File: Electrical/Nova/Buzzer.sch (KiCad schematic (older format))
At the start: 2 parts, among them IC1201 74HC2GU04GW,125

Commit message: Deleted Inverter
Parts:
- removed IC1201: 74HC2GU04GW,125, Footprint Library:SOP65P210X110-6N, symbol Nova-rescue:74HC2GU04GW,125-74HC2GU04GW_125-Nova-rescue-Nova-rescue-Nova-rescue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
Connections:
- net labels removed: +3V3
- wire segments 15 -> 2
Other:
- moved on the sheet: LS1201
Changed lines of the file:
@@
 $Descr A4 11693 8268
 encoding utf-8
-Sheet 12 19
+Sheet 3 19
 Title ""
 Date ""
@@
 L Nova-rescue:PS1440P02BT-PS1440P02BT-Nova-rescue-Nova-rescue-Nova-rescue-Nova-rescue-Nova-rescue LS1201
 U 1 1 5F404605
-P 5450 3800
-F 0 "LS1201" H 5580 3846 50  0000 L CNN
-F 1 "PS1440P02BT" H 5580 3755 50  0000 L CNN
-F 2 "Footprint Library:BUZZER_PS1440P02BT" H 5450 3800 50  0001 L BNN
-F 3 "https://product.tdk.com/info/en/catalog/datasheets/piezoelectronic_buzzer_ps_en.pdf" H 5450 3800 50  0001 L BNN
-F 4 "IPC-7251" H 5450 3800 50  0001 L BNN "Field4"
-	1    5450 3800
+P 5750 3450
+F 0 "LS1201" H 5880 3496 50  0000 L CNN
+F 1 "PS1440P02BT" H 5880 3405 50  0000 L CNN
+F 2 "Footprint Library:BUZZER_PS1440P02BT" H 5750 3450 50  0001 L BNN
+F 3 "https://product.tdk.com/info/en/catalog/datasheets/piezoelectronic_buzzer_ps_en.pdf" H 5750 3450 50  0001 L BNN
+F 4 "IPC-7251" H 5750 3450 50  0001 L BNN "Field4"
+	1    5750 3450
 	0    1    1    0
-$EndComp
-$Comp
-L Nova-rescue:74HC2GU04GW,125-74HC2GU04GW_125-Nova-rescue-Nova-rescue-Nova-rescue-Nova-rescue-Nova-rescue IC?
-U 1 1 5F40586B
-P 4950 3100
-AR Path="/5F40586B" Ref="IC?"  Part="1"
-AR Path="/5F36176A/5F40586B" Ref="IC1201"  Part="1"
-F 0 "IC1201" H 5450 3365 50  0000 C CNN
-F 1 "74HC2GU04GW,125" H 5450 3274 50  0000 C CNN
-F 2 "Footprint Library:SOP65P210X110-6N" H 5800 3200 50  0001 L CNN
-F 3 "https://assets.nexperia.com/documents/data-sheet/74HC2GU04.pdf" H 5800 3100 50  0001 L CNN
-F 4 "74HC2GU04 - Dual unbuffered inverter@en-us" H 5800 3000 50  0001 L CNN "Description"
-F 5 "1.1" H 5800 2900 50  0001 L CNN "Height"
-F 6 "Nexperia" H 5800 2800 50  0001 L CNN "Manufacturer_Name"
-F 7 "74HC2GU04GW,125" H 5800 2700 50  0001 L CNN "Manufacturer_Part_Number"
-F 8 "74HC2GU04GW,125" H 5800 2600 50  0001 L CNN "Arrow Part Number"
-F 9 "https://www.arrow.com/en/products/74hc2gu04gw125/nexperia" H 5800 2500 50  0001 L CNN "Arrow Price/Stock"
-F 10 "" H 5800 2400 50  0001 L CNN "Mouser Part Number"
-F 11 "" H 5800 2300 50  0001 L CNN "Mouser Price/Stock"
-	1    4950 3100
-	1    0    0    -1
 $EndComp
 $Comp
 L power:GND #PWR01201
 U 1 1 5F407098
-P 4750 3200
-F 0 "#PWR01201" H 4750 2950 50  0001 C CNN
-F 1 "GND" V 4755 3072 50  0000 R CNN
-F 2 "" H 4750 3200 50  0001 C CNN
-F 3 "" H 4750 3200 50  0001 C CNN
-	1    4750 3200
+P 5250 3350
+F 0 "#PWR01201" H 5250 3100 50  0001 C CNN
+F 1 "GND" V 5255 3222 50  0000 R CNN
+F 2 "" H 5250 3350 50  0001 C CNN
+F 3 "" H 5250 3350 50  0001 C CNN
+	1    5250 3350
 	0    1    1    0
 $EndComp
-Wire Wire Line
-	4950 3200 4750 3200
-$Comp
-L power:+3V3 #PWR01202
-U 1 1 5F4096B6
-P 6150 3200
-F 0 "#PWR01202" H 6150 3050 50  0001 C CNN
-F 1 "+3V3" V 6165 3328 50  0000 L CNN
-F 2 "" H 6150 3200 50  0001 C CNN
-F 3 "" H 6150 3200 50  0001 C CNN
-	1    6150 3200
-	0    1    1    0
-$EndComp
-Wire Wire Line
-	5950 3100 6500 3100
-Wire Wire Line
-	6500 3700 5650 3700
-Wire Wire Line
-	4700 3100 4950 3100
-Wire Wire Line
-	6500 3100 6500 3600
-Wire Wire Line
-	5250 3700 5100 3700
-Wire Wire Line
-	5100 3700 5100 3500
-Wire Wire Line
-	5100 3500 6100 3500
-Wire Wire Line
-	6100 3500 6100 3300
-Wire Wire Line
-	6100 3300 5950 3300
-Wire Wire Line
-	4950 3300 4800 3300
-Wire Wire Line
-	4800 3300 4800 3600
-Wire Wire Line
-	4800 3600 6500 3600
-Connection ~ 6500 3600
-Wire Wire Line
-	6500 3600 6500 3700
-Text HLabel 4700 3100 0    50   Input ~ 0
+Text HLabel 6300 3350 2    50   Input ~ 0
 BUZZER
 Wire Wire Line
-	5950 3200 6150 3200
+	5250 3350 5550 3350
+Wire Wire Line
+	5950 3350 6300 3350
 $EndSCHEMATC

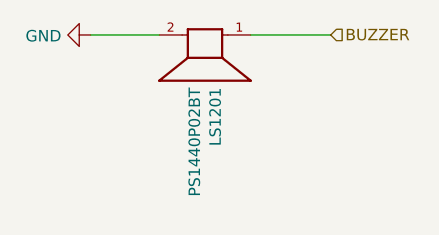
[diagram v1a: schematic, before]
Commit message: Reorganized Schematic and Connected CS pins (0603)
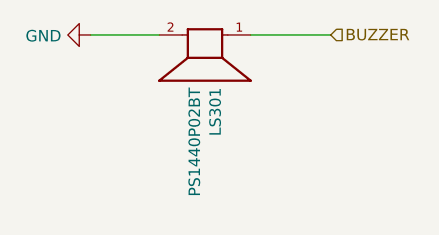
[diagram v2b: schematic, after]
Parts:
- renumbered LS1201 to LS301
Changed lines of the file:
@@
 $EndDescr
 $Comp
-L Nova-rescue:PS1440P02BT-PS1440P02BT-Nova-rescue-Nova-rescue-Nova-rescue-Nova-rescue-Nova-rescue LS1201
+L Nova-rescue:PS1440P02BT-PS1440P02BT-Nova-rescue-Nova-rescue-Nova-rescue-Nova-rescue-Nova-rescue LS301
 U 1 1 5F404605
 P 5750 3450
-F 0 "LS1201" H 5880 3496 50  0000 L CNN
+F 0 "LS301" H 5880 3496 50  0000 L CNN
 F 1 "PS1440P02BT" H 5880 3405 50  0000 L CNN
 F 2 "Footprint Library:BUZZER_PS1440P02BT" H 5750 3450 50  0001 L BNN
@@
 $EndComp
 $Comp
-L power:GND #PWR01201
+L power:GND #PWR0301
 U 1 1 5F407098
 P 5250 3350
-F 0 "#PWR01201" H 5250 3100 50  0001 C CNN
+F 0 "#PWR0301" H 5250 3100 50  0001 C CNN
 F 1 "GND" V 5255 3222 50  0000 R CNN
 F 2 "" H 5250 3350 50  0001 C CNN

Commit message: Minor Layout Change
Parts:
- LS301: footprint Footprint Library:BUZZER_PS1440P02BT -> Transducer:BUZZER_PS1440P02BT
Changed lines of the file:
@@
 F 0 "LS301" H 5880 3496 50  0000 L CNN
 F 1 "PS1440P02BT" H 5880 3405 50  0000 L CNN
-F 2 "Footprint Library:BUZZER_PS1440P02BT" H 5750 3450 50  0001 L BNN
+F 2 "Transducer:BUZZER_PS1440P02BT" H 5750 3450 50  0001 L BNN
 F 3 "https://product.tdk.com/info/en/catalog/datasheets/piezoelectronic_buzzer_ps_en.pdf" H 5750 3450 50  0001 L BNN
 F 4 "IPC-7251" H 5750 3450 50  0001 L BNN "Field4"

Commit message: Updated Voltage Regulators
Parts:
- LS301: symbol Nova-rescue:PS1440P02BT-PS1440P02BT-Nova-rescue-Nova-rescue-Nova-rescue-Nova-rescue-Nova-rescue -> Nova-rescue:PS1440P02BT-PS1440P02BT-Nova-rescue-Nova-rescue-Nova-rescue-Nova-rescue-Nova-rescue-Nova-rescue
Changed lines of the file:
@@
 $EndDescr
 $Comp
-L Nova-rescue:PS1440P02BT-PS1440P02BT-Nova-rescue-Nova-rescue-Nova-rescue-Nova-rescue-Nova-rescue LS301
+L Nova-rescue:PS1440P02BT-PS1440P02BT-Nova-rescue-Nova-rescue-Nova-rescue-Nova-rescue-Nova-rescue-Nova-rescue LS301
 U 1 1 5F404605
 P 5750 3450
+AR Path="/5F404605" Ref="LS301"  Part="1"
+AR Path="/5F36176A/5F404605" Ref="LS301"  Part="1"
 F 0 "LS301" H 5880 3496 50  0000 L CNN
 F 1 "PS1440P02BT" H 5880 3405 50  0000 L CNN

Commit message: Added Pin header
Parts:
- LS301: symbol Nova-rescue:PS1440P02BT-PS1440P02BT-Nova-rescue-Nova-rescue-Nova-rescue-Nova-rescue-Nova-rescue-Nova-rescue -> Nova-rescue:PS1440P02BT-PS1440P02BT-Nova-rescue-Nova-rescue-Nova-rescue-Nova-rescue-Nova-rescue-Nova-rescue-Nova-rescue
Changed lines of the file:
@@
 $Descr A4 11693 8268
 encoding utf-8
-Sheet 3 19
+Sheet 3 20
 Title ""
 Date ""
@@
 $EndDescr
 $Comp
-L Nova-rescue:PS1440P02BT-PS1440P02BT-Nova-rescue-Nova-rescue-Nova-rescue-Nova-rescue-Nova-rescue-Nova-rescue LS301
+L Nova-rescue:PS1440P02BT-PS1440P02BT-Nova-rescue-Nova-rescue-Nova-rescue-Nova-rescue-Nova-rescue-Nova-rescue-Nova-rescue LS301
 U 1 1 5F404605
 P 5750 3450

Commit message: Minor Fixes and Additions
Fixed Symbol Library for Buzzer and Voltage Regulator. Also added a resistor for the Pyro 1mF cap
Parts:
- LS301: symbol Nova-rescue:PS1440P02BT-PS1440P02BT-Nova-rescue-Nova-rescue-Nova-rescue-Nova-rescue-Nova-rescue-Nova-rescue-Nova-rescue -> Device:Buzzer
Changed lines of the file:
@@
 $EndDescr
 $Comp
-L Nova-rescue:PS1440P02BT-PS1440P02BT-Nova-rescue-Nova-rescue-Nova-rescue-Nova-rescue-Nova-rescue-Nova-rescue-Nova-rescue LS301
+L Device:Buzzer LS301
 U 1 1 5F404605
 P 5750 3450
@@
 BUZZER
 Wire Wire Line
-	5250 3350 5550 3350
+	5850 3350 6300 3350
 Wire Wire Line
-	5950 3350 6300 3350
+	5250 3350 5650 3350
 $EndSCHEMATC
